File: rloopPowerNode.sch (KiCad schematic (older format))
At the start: 93 parts, among them P1 CONN_01X02, P10 CONN_01X03, P11 CONN_01X03, P13 CONN_01X03, P14 CONN_01X03, P15 CONN_01X01, P16 CONN_01X01, P17 CONN_01X08, P18 CONN_01X02, P19 CONN_01X02, P2 CONN_01X02, P20 CONN_01X02, P21 CONN_01X02, P22 AMPMODU-02X05, P23 SHUNT, P3 CONN_01X02, P4 CONN_01X02, P5 CONN_01X01, P6 CONN_01X04, P7 CONN_01X02, P8 CONN_01X02, P9 CONN_01X02, Q1 PMOS, Q2 NMOS, Q3 BSS84, U1 CPC1718, U10 AMC1100, U2 CPC1718, U3 H11F1SM, U4 MAX6814, U5 CPC1718, U6 CPC1718, U7 DS2482-100, U8 MS5607-02BA03, U9 78L05

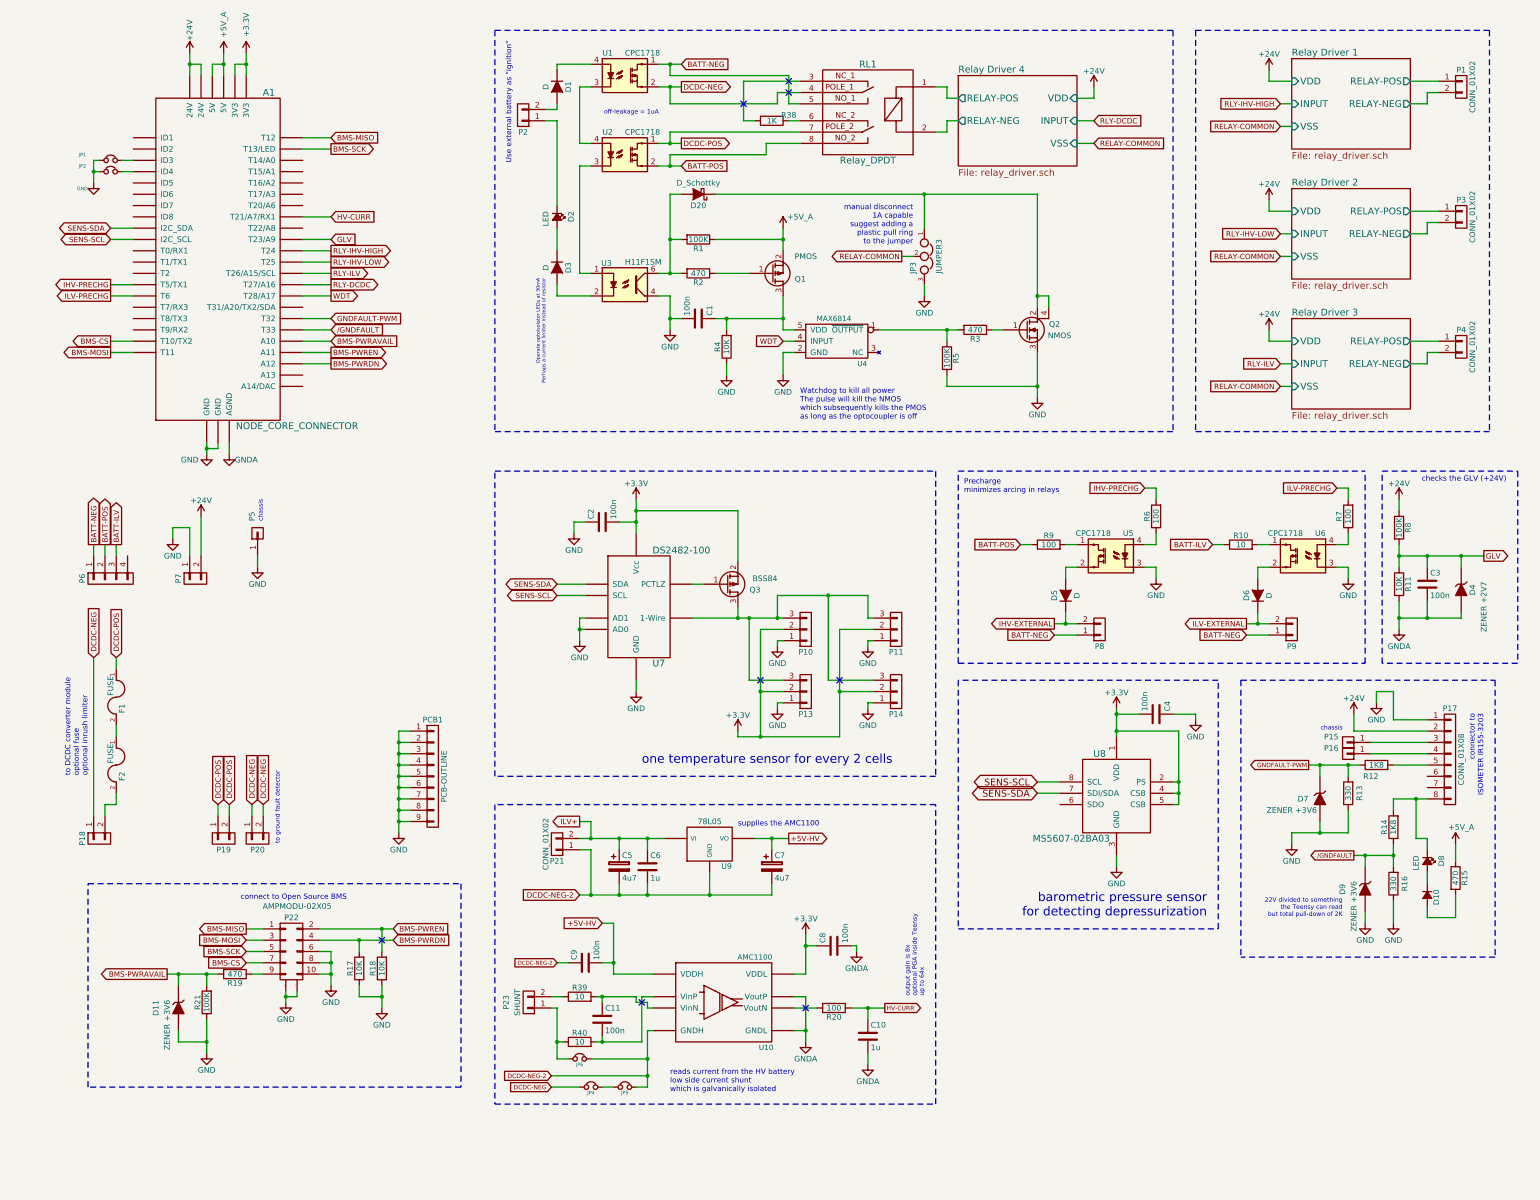
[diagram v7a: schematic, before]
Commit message: added backup hookups/testpoints, a lot more routing
subcircuits are essentially complete except the BMS mount and the node
core, the hookups are a backup in case the node core doesn't get
finished
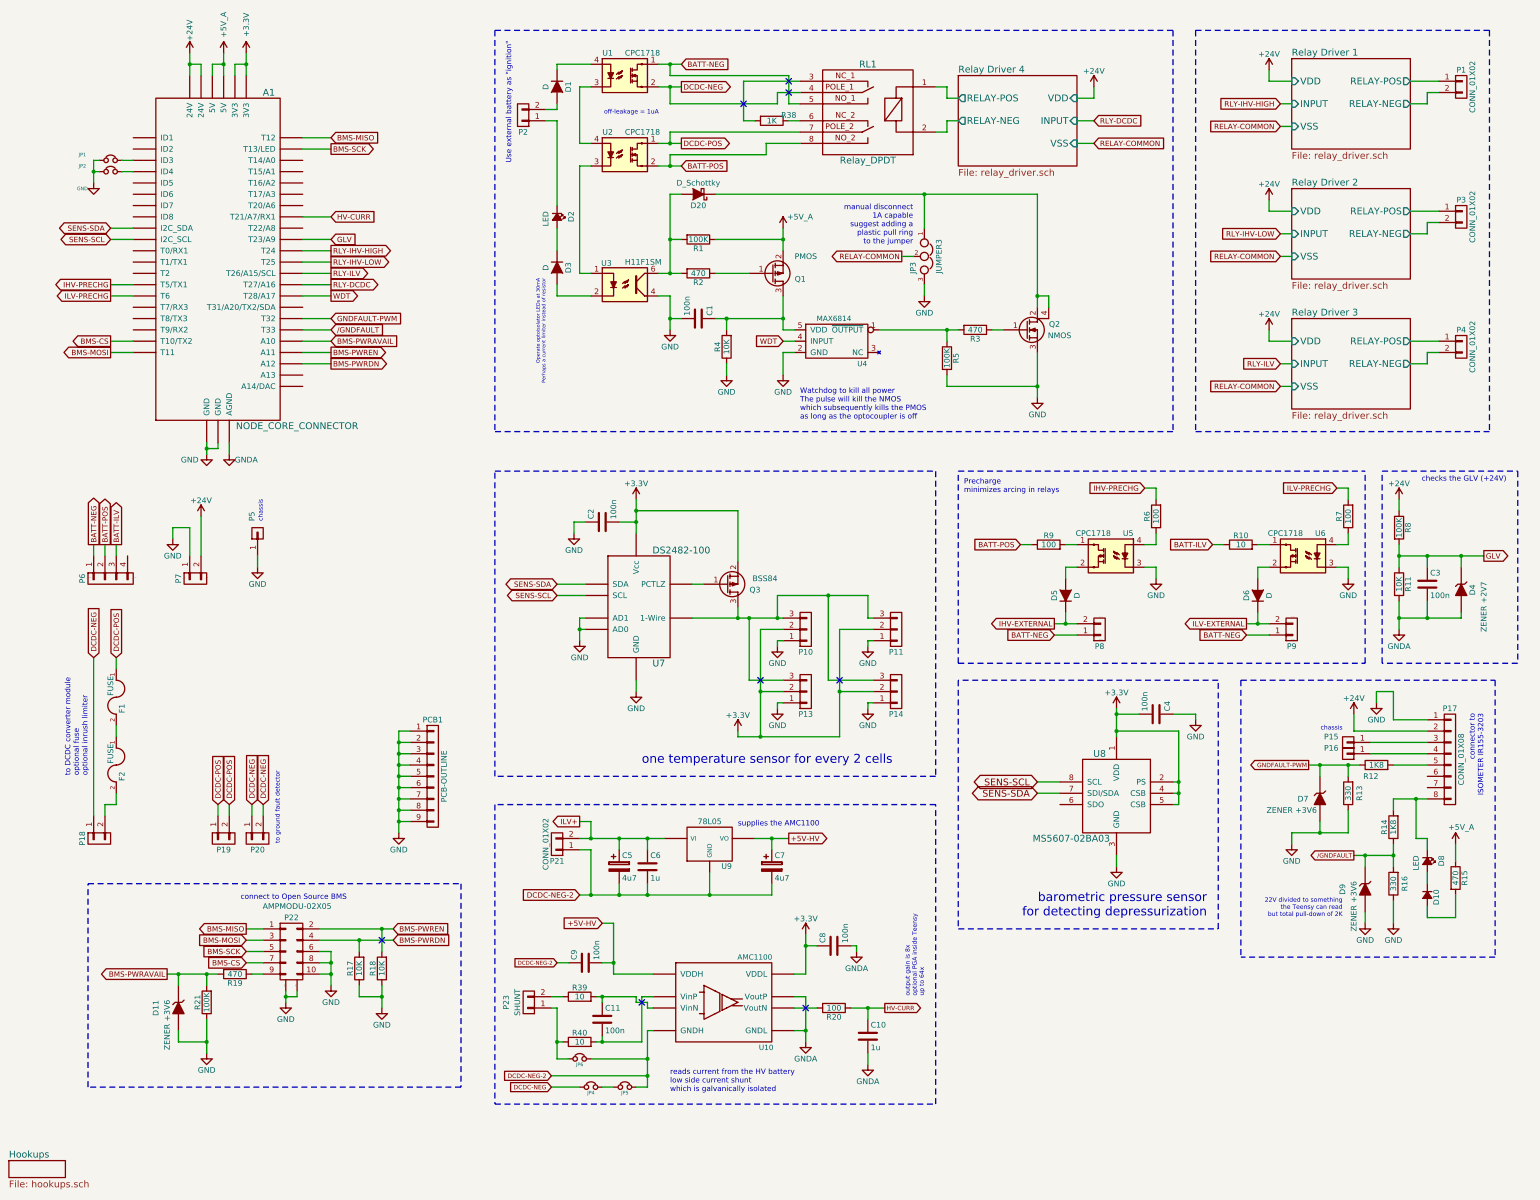
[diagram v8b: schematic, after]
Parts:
- A1: footprint (none) -> -footprints:NODE-CORE
- JP4, JP5: footprint -footprints:SOLDERJUMPER -> Resistors_SMD:R_1206_HandSoldering
